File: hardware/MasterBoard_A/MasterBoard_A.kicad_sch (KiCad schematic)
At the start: 53 parts, among them J1 Conn_01x09_Socket, J2 Conn_02x05_Odd_Even, J3 Global LV and CAN, J4 Conn_01x02_Socket, J6 HRLV, J7 Main Current Hall Sensor, J9 PWM sig bank 1, K2 G5Q-1A, Q1 MMBT5550L, Q2 MMBT5550L, Q9 MMBT5550L, SW1 SW_Push, U10 MCP9700x-ETT, U13 MCP2542FDxMF, U2 MCU-MSM0G3507SPM, U22 MCP9700x-ETT, U6 MCP2542FDxMF

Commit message: mb 1.1 on da way. more shuffling
trying to be more professional about the part choices. obtuse excel sheet of pain has arrived.
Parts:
- removed C15: 220n, Capacitor_SMD:C_0805_2012Metric_Pad1.18x1.45mm_HandSolder, symbol Device:C_Small
- removed C26: 100n, Capacitor_SMD:C_1206_3216Metric_Pad1.33x1.80mm_HandSolder, symbol Device:C_Small
- removed C5: 10n, Capacitor_SMD:C_0805_2012Metric_Pad1.18x1.45mm_HandSolder, symbol Device:C_Small
- removed J1: Conn_01x09_Socket, Connector_PinHeader_2.54mm:PinHeader_1x09_P2.54mm_Vertical, symbol Connector:Conn_01x09_Socket
- removed J4: Conn_01x02_Socket, Connector_PinHeader_2.54mm:PinHeader_1x02_P2.54mm_Vertical, symbol Connector:Conn_01x02_Socket
- removed K2: G5Q-1A, Relay_THT:Relay_SPST_Omron-G5Q-1A, symbol Relay:G5Q-1A
- removed R10, R3, R56: 3.32k, Resistor_SMD:R_0805_2012Metric_Pad1.20x1.40mm_HandSolder, symbol Device:R_Small_US
- removed R41: 3.3, Resistor_SMD:R_1206_3216Metric_Pad1.30x1.75mm_HandSolder, symbol Device:R_Small_US
- removed U2: MCU-MSM0G3507SPM, zzLocalLibraries-Footprints:MSPM0G3507-64-IPC_A, symbol zzLocalLibrary:MCU-MSM0G3507SPM
- added C105: 220n, Capacitor_SMD:C_0805_2012Metric_Pad1.18x1.45mm_HandSolder, symbol Device:C_Small
- added J104: uart, Connector_PinHeader_2.54mm:PinHeader_1x03_P2.54mm_Vertical, symbol Connector:Conn_01x03_Pin
- added K101: G5Q-1A 24Vdc, Relay_THT:Relay_SPST_Omron-G5Q-1A, symbol Relay:G5Q-1A
- added R101, R102, R107: 2.4k, Resistor_SMD:R_0805_2012Metric_Pad1.20x1.40mm_HandSolder, symbol Device:R_Small_US
- added R114: 332, Resistor_SMD:R_1206_3216Metric_Pad1.30x1.75mm_HandSolder, symbol Device:R_Small_US
- added U102: XM0G3507QPTRQ1, zzLocalLibraries-Footprints:PT0048A-IPC_B, symbol zzLocalLibrary:XM0G3507QPTRQ1
- J102: renamed from J9; now not fitted; now left out of the parts list
- renumbered C14 to C101, C13 to C102, C43 to C103, C11 to C104, C9 to C106, C7 to C107, D26 to D101, D20 to D102, D11 to D103, D24 to D104, D5 to D105, D23 to D106, F1 to F101, H4 to H101, H5 to H102, J3 to J101, J2 to J103, J6 to J105, J7 to J106, Q9 to Q101, Q2 to Q102, Q1 to Q103, R25 to R103, R8 to R104, R30 to R105, R12 to R106, R7 to R108, R5 to R109, R31 to R110, R1 to R111, R26 to R112, R24 to R113, SW1 to SW101, TP1 to TP101, TP3 to TP102, TP4 to TP103, TP9 to TP104, U13 to U101, U6 to U103, U10 to U104, U22 to U105
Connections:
- net +3.3V: now also U102.6 (VDD)
- net GND: now also C105.2, J104.1 (Pin_1), R101.2, R102.2, R107.2, U102.7 (VSS)
- net G_IL+: now also K101.3
- net G_IL-: now also K101.2
- net LV+: now also K101.1
- net XDS_RESET_OUT: no longer R108.1, SW101.1
- net XDS_RXD: now also J104.2 (Pin_2)
- net XDS_TXD: now also J104.3 (Pin_3)
- net obtherm.1: now also R114.1
- net at D103.2 (A), Q103.3 (C): now also K101.5
- net at D104.1 (K): now also R107.1
- net at U105.2 (V_{OUT}): now also R114.2
- net at R104.2: now also U102.8 (PA2_ROSC)
- net at D102.1 (K): now also R102.1
- net at D101.1 (K): now also R101.1
- net Vcore: no longer names the net of C104.1
- net Vcore: now also C105.1, U102.48 (VCORE)
- new net: R108.1, SW101.1, U102.4 (RST_N)
- no-connect marks 43 -> 7
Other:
- note added: "SWD fish"
- note removed: "Avoid using port B. THe smaller chip models usually cut it first"
- note removed: "JTAG"
- note removed: "Programming"
- note removed: "TODO: rearrange for bus, conns direct connect to bus. for better visi"
- note removed: "XDS110 specific"
- note removed: "in this caes port B only used for GPIO connections"
- note removed: "reset btn"
- note removed: "user uart"
- moved on the sheet: C101, C102, C104, C106, D101, D102, D104, D105, D106, H101, H102, J103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

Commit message: excel monkey has monkey do-ne it
eyeballed a format for the psu table, it gets the point across
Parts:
- removed J105: HRLV, Connector_Molex:Molex_Micro-Fit_3.0_43650-0500_1x05_P3.00mm_Horizontal, symbol Connector:Conn_01x05_Pin
- removed R103: 97.6k, Resistor_SMD:R_0805_2012Metric_Pad1.20x1.40mm_HandSolder, symbol Device:R_Small_US
- removed R112, R113: 3.3, Resistor_SMD:R_1206_3216Metric_Pad1.30x1.75mm_HandSolder, symbol Device:R_Small_US
- removed R114: 332, Resistor_SMD:R_1206_3216Metric_Pad1.30x1.75mm_HandSolder, symbol Device:R_Small_US
- removed U104: MCP9700x-ETT, Package_TO_SOT_SMD:SOT-23-3, symbol Sensor_Temperature:MCP9700x-ETT
- added C103, C104, C106, C107: 220n, Capacitor_SMD:C_0805_2012Metric_Pad1.18x1.45mm_HandSolder, symbol Device:C_Small
- added J103: HRLV, Connector_Molex:Molex_Micro-Fit_3.0_43045-0600_2x03_P3.00mm_Horizontal, symbol Connector_Generic:Conn_02x03_Top_Bottom
- added R101: 40.2k, Resistor_SMD:R_0805_2012Metric_Pad1.20x1.40mm_HandSolder, symbol Device:R_Small_US
- added R104: 88.7k, Resistor_SMD:R_0805_2012Metric_Pad1.20x1.40mm_HandSolder, symbol Device:R_Small_US
- added U103: MCP9700x-ETT, Package_TO_SOT_SMD:SOT-23-3, symbol Sensor_Temperature:MCP9700x-ETT
- R105: value 10k -> 3.32k; mouser https://www.mouser.com/ProductDetail/YAGEO/AC0805FR-7W10KL?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 -> https://www.mouser.com/ProductDetail/Walsin/WR08X3321FTL?qs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; specs 10k , 250mW, 150V, 1%, 100ppm, -55C, +155C -> 3.32kOhm, 1%, 150V, 125mW, 100ppm, -55C, 155C; unit x1 0.1 -> 0.10; unit x10 0.015 -> 0.019
- renumbered C103 to C101, C107 to C102, C106 to C105, C101 to C108, C104 to C109, C102 to C110, C105 to C111, D103 to D101, D105 to D102, D101 to D103, D102 to D104, D104 to D105, J106 to J101, J101 to J102, J102 to J104, J103 to J105, J104 to J106, Q103 to Q101, Q101 to Q103, R109 to R102, R111 to R103, R101 to R107, R102 to R108, R107 to R109, R104 to R111, R108 to R112, TP104 to TP101, TP101 to TP102, TP102 to TP103, TP103 to TP104, U103 to U102, U105 to U104, U102 to U105
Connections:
- net +3.3V: now also C103.1, C104.1, C106.1, C107.1, U103.1 (V_{DD})
- net GND: now also C103.2, C104.2, C106.2, C107.2, R101.1, U103.3 (GND)
- net G_IL+: now also R104.2
- net obtherm.1: now also U104.2 (V_{OUT})
- net at R103.2, U102.8 (STBY): no longer U101.8 (STBY)
- net at Q102.1 (B), Q103.1 (B), R105.2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: now also R104.1
- new net: R101.2, U101.8 (STBY)
- new net HRLV_CAN+: J103.4 (Pin_4)
- new net HRLV_CAN-: J103.1 (Pin_1)
- new net HRLV_IL+: J103.2 (Pin_2)
- new net HRLV_IL-: J103.5 (Pin_5)
- new net HRLV_LV+: J103.6 (Pin_6)
- new net HRLV_LV-: J103.3 (Pin_3)
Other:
- sheet HRLV interface ports: added HRLV_IL+, HRLV_IL-, VDD, VSS; removed HRLV_IL, SIG+, SIG-
- sheet Main Current Hall Sensing ports: added MCHS_shutdown_N, SDI; removed none
- note added: "CAN and IL are swapped to fail if the GLV connector is used"
- note added: "Scheduler running"
- note removed: "RTOS running"
- moved on the sheet: C105

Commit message: multi channel propaganda
only bots use multi channel layouts
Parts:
- removed C101: 1n 2kV, Capacitor_SMD:C_1206_3216Metric_Pad1.33x1.80mm_HandSolder, symbol Device:C_Small
- removed D101: ES1D, Diode_SMD:D_SMA, symbol Device:D_Schottky_Small
- added D101: TS4148, Diode_SMD:D_0805_2012Metric_Pad1.15x1.40mm_HandSolder, symbol Device:D_Small
- added H103: MountingHole, MountingHole:MountingHole_3.2mm_M3, symbol Mechanical:MountingHole
- H101, H102: footprint MountingHole:MountingHole_3.2mm_M3_Pad_Via -> MountingHole:MountingHole_3.2mm_M3
- renumbered C102 to C101, C103 to C102, C104 to C103, C105 to C104, C106 to C105, C107 to C106, C108 to C107, C109 to C108, C110 to C109, C111 to C110
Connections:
- net G_IL_I is gone; now on net GLV-: J102.2 (Pin_2)
- net G_IL_O is gone; now on net GLV+: J102.5 (Pin_5)
- net GLV+: no longer J102.6 (Pin_6)
- net GLV-: no longer J102.3 (Pin_3)
- net G_CAN_+: now also J102.3 (Pin_3); no longer J102.1 (Pin_1)
- net G_CAN_-: now also J102.6 (Pin_6); no longer J102.4 (Pin_4)
- net G_IL+: now also J102.1 (Pin_1)
- net G_IL-: now also J102.4 (Pin_4)
- net LV+: now also D101.1 (K)
- net at K101.5, Q101.3 (C): now also D101.2 (A)
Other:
- moved on the sheet: H101

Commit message: saturn tool kit my beloved
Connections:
- net HRLV_CAN+: now also J103.1 (Pin_1); no longer J103.4 (Pin_4)
- net HRLV_CAN-: now also J103.4 (Pin_4); no longer J103.1 (Pin_1)
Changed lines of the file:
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@@
 	)
 	(label "HRLV_CAN-"
-		(at 24.13 151.13 180)
+		(at 36.83 151.13 0)
 		(effects
 			(font
 				(size 1.27 1.27)
 			)
-			(justify right bottom)
+			(justify left bottom)
 		)
 	)
@@
 	)
 	(label "HRLV_CAN+"
-		(at 36.83 151.13 0)
+		(at 24.13 151.13 180)
 		(effects
 			(font
 				(size 1.27 1.27)
 			)
-			(justify left bottom)
+			(justify right bottom)
 		)
 	)

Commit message: mb layout: all but mcu bundle
thou who completes thy layout must endure excel
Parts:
- removed C103: 220n, Capacitor_SMD:C_0805_2012Metric_Pad1.18x1.45mm_HandSolder, symbol Device:C_Small
- removed R101, R103: 40.2k, Resistor_SMD:R_0805_2012Metric_Pad1.20x1.40mm_HandSolder, symbol Device:R_Small_US
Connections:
- net G_CAN_+ is gone; now on net G_CAN-: J102.3 (Pin_3)
- net G_CAN_- is gone; now on net G_CAN+: J102.6 (Pin_6)
- net GND: now also U101.8 (STBY), U102.8 (STBY)

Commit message: mb ready for review
one of yall poor souls has to verify the schematic and layout
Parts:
- removed TP101: TestPoint, TestPoint:TestPoint_THTPad_3.0x3.0mm_Drill1.5mm, symbol Connector:TestPoint
- added R1, R2: 100, Resistor_SMD:R_1206_3216Metric_Pad1.30x1.75mm_HandSolder, symbol Device:R_Small_US
- C106, SW101, U104: now not fitted; now left out of the parts list
- TP102, TP103, TP104: now not fitted
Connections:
- net +3.3V: now also U105.36 (PB17_A1_4), U105.5 (PA31_CLK_OUT)
- net GND: now also D103.1 (K), D105.1 (K), U105.23 (PB9); no longer R107.2, R109.2
- net IL.forward: now also U105.22 (PB8)
- net IL.sense: now also U105.21 (PB7)
- net XDS_RXD: now also U105.39 (PA21_A1_7_VREF-)
- net XDS_TCK_SWDCLK: now also U105.35 (PA20_SWCLK)
- net XDS_TMS_SWDIO: now also U105.34 (PA19_SWDIO)
- net XDS_TXD: now also U105.40 (PA22_CLK_OUT_A0_7)
- net can.rx: now also U105.47 (PA27_RTC_OUT_A0_0)
- net can.tx: now also U105.46 (PA26_A0_1)
- net eth.MISO/POCI: now also U105.28 (PA13)
- net eth.MOSI/PICO: now also U105.29 (PA14_CLK_OUT_A0_12)
- net eth.SCLK: now also U105.27 (PA12_FCC_IN)
- net eth.cs_N: now also U105.30 (PA15_A1_0)
- net eth.irq_N: now also U105.25 (PB15)
- net eth.reset_N: now also U105.24 (PB14)
- net hrlv.pres_hrlv: now also U105.41 (PB20_A0_6)
- net hrlv.pres_interlock: now also U105.42 (PB24_A0_5)
- net led.BMSFault: now also R109.2, U105.11 (PA5_HFXIN_FCC_IN); no longer D105.2 (A)
- net led.i1: now also U105.44 (PA24_A0_3)
- net led.i2: now also R107.2, U105.12 (PA6_HFCLK_IN_HFXOUT); no longer D103.2 (A)
- net led.sched: now also U105.43 (PA23_VREF+)
- net mchs.MISO/POCI: now also U105.31 (PA16_A1_1_FCC_IN), R1.2
- net mchs.MOSI/PICO: now also U105.33 (PA18_A1_3)
- net mchs.SCLK: now also U105.32 (PA17_A1_2), R2.2
- net mchs.cs_imp: now also U105.38 (PB19_A1_6)
- net mchs.cs_per: now also U105.37 (PB18_A1_5)
- net vcore: now reaches C108.1, C110.1, U105.48 (VCORE)
- net at R107.1: now also D103.2 (A); no longer D103.1 (K)
- net at R109.1: now also D105.2 (A); no longer D105.1 (K)
- new net Main Current Hall Sensing/SCLK: R2.1
- new net Main Current Hall Sensing/SDO: R1.1
- no-connect marks 7 -> 24
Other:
- sheet HRLV interface ports: added none; removed VSS
- moved on the sheet: D103, D105, R107, R109

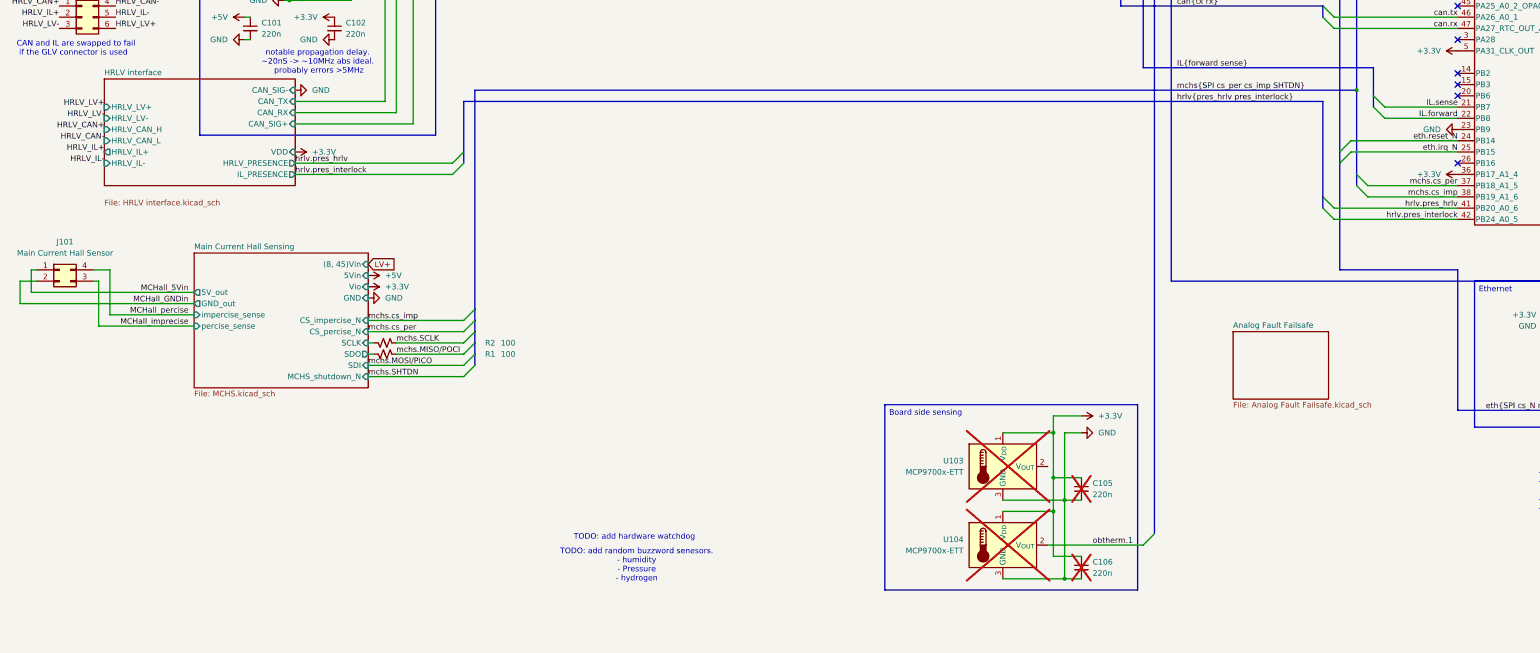
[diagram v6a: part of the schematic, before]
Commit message: master board shuffling
jlc says $2. yippie
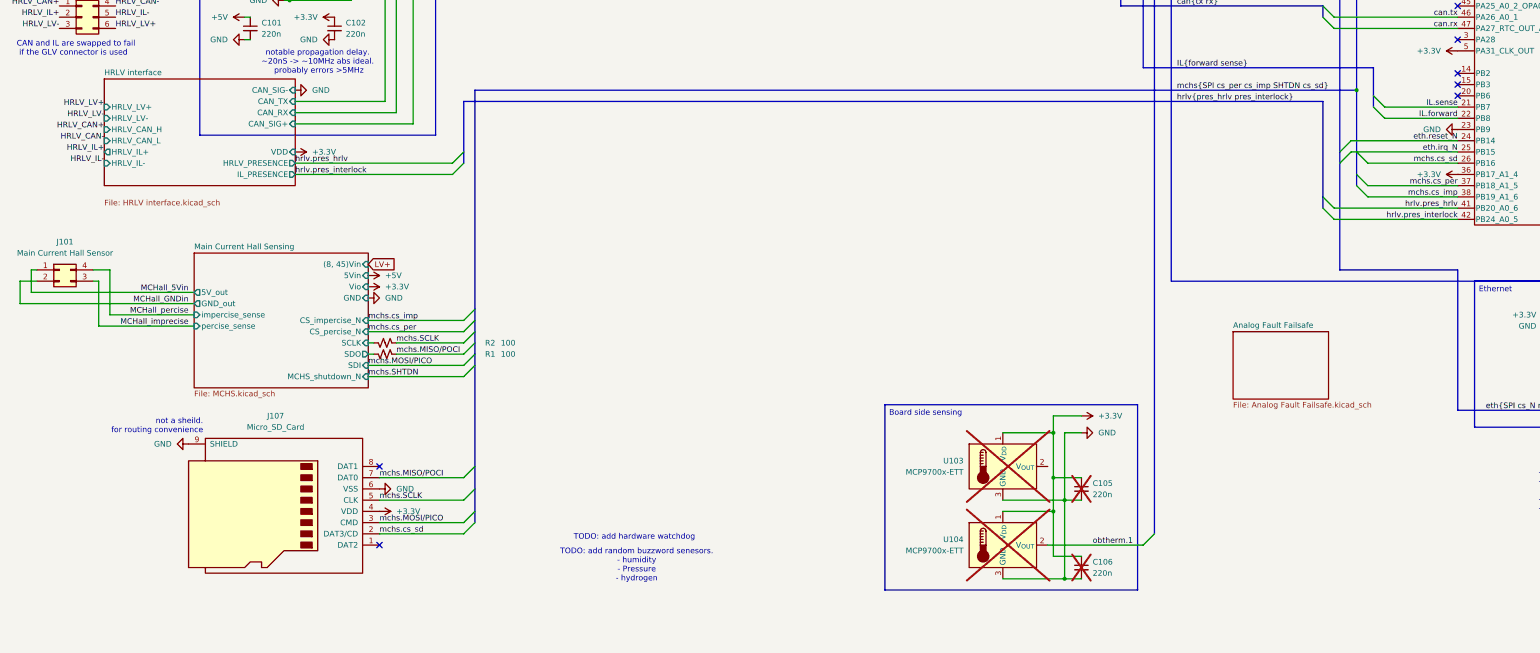
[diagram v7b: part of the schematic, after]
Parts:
- added J107: Micro_SD_Card, Connector_Card:microSD_HC_Wuerth_693072010801, symbol Connector:Micro_SD_Card
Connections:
- net +3.3V: now also J107.4 (VDD)
- net GND: now also J107.6 (VSS), J107.9 (SHIELD)
- net mchs.MISO/POCI: now also J107.7 (DAT0)
- net mchs.MOSI/PICO: now also J107.3 (CMD)
- net mchs.SCLK: now also J107.5 (CLK)
- net mchs.cs_sd: now reaches U105.26 (PB16)
- net mchs.cs_sd: now also J107.2 (DAT3/CD)
- no-connect marks 24 -> 25
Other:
- note added: "not a sheild. for routing convenience"

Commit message: me when i forget a wire
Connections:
- net XDS_RXD: now also J106.3 (Pin_3); no longer J106.2 (Pin_2)
- net XDS_TXD: now also J106.2 (Pin_2); no longer J106.3 (Pin_3)
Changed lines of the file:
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@@
+	)
+	(junction
+		(at 382.27 50.8)
+		(diameter 0)
+		(color 0 0 0 0)
 	)
 	(junction
@@
 	)
 	(junction
-		(at 382.27 50.8)
-		(diameter 0)
-		(color 0 0 0 0)
-	)
-	(junction
 		(at 189.23 39.37)
 		(diameter 0)
@@
 	(wire
 		(pts
+			(xy 384.81 53.34) (xy 387.35 53.34)
+		)
+		(stroke
+			(width 0)
+			(type default)
+		)
+	)
+	(wire
+		(pts
 			(xy 93.98 60.96) (xy 83.82 60.96)
 		)
@@
 	(wire
 		(pts
+			(xy 389.89 53.34) (xy 387.35 50.8)
+		)
+		(stroke
+			(width 0)
+			(type default)
+		)
+	)
+	(wire
+		(pts
 			(xy 134.62 53.34) (xy 133.35 53.34)
 		)
@@
 		)
 	)
-	(wire
-		(pts
-			(xy 384.81 53.34) (xy 391.16 53.34)
-		)
-		(stroke
-			(width 0)
-			(type default)
-		)
-	)
 	(bus
 		(pts
@@
 	(wire
 		(pts
+			(xy 389.89 50.8) (xy 391.16 50.8)
+		)
+		(stroke
+			(width 0)
+			(type default)
+		)
+	)
+	(wire
+		(pts
 			(xy 185.42 69.85) (xy 189.23 69.85)
 		)
@@
 	(wire
 		(pts
+			(xy 382.27 50.8) (xy 387.35 50.8)
+		)
+		(stroke
+			(width 0)
+			(type default)
+		)
+	)
+	(wire
+		(pts
 			(xy 85.09 73.66) (xy 85.09 72.39)
 		)
@@
 		)
 	)
-	(wire
-		(pts
-			(xy 382.27 50.8) (xy 391.16 50.8)
-		)
-		(stroke
-			(width 0)
-			(type default)
-		)
-	)
 	(bus
 		(pts
@@
 	(wire
 		(pts
+			(xy 389.89 50.8) (xy 387.35 53.34)
+		)
+		(stroke
+			(width 0)
+			(type default)
+		)
+	)
+	(wire
+		(pts
 			(xy 312.42 146.05) (xy 340.36 146.05)
 		)
@@
 		)
 		(stroke
+			(width 0)
+			(type default)
+		)
+	)
+	(wire
+		(pts
+			(xy 391.16 53.34) (xy 389.89 53.34)
+		)
+		(stroke
